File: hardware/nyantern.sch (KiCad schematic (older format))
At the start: 23 parts

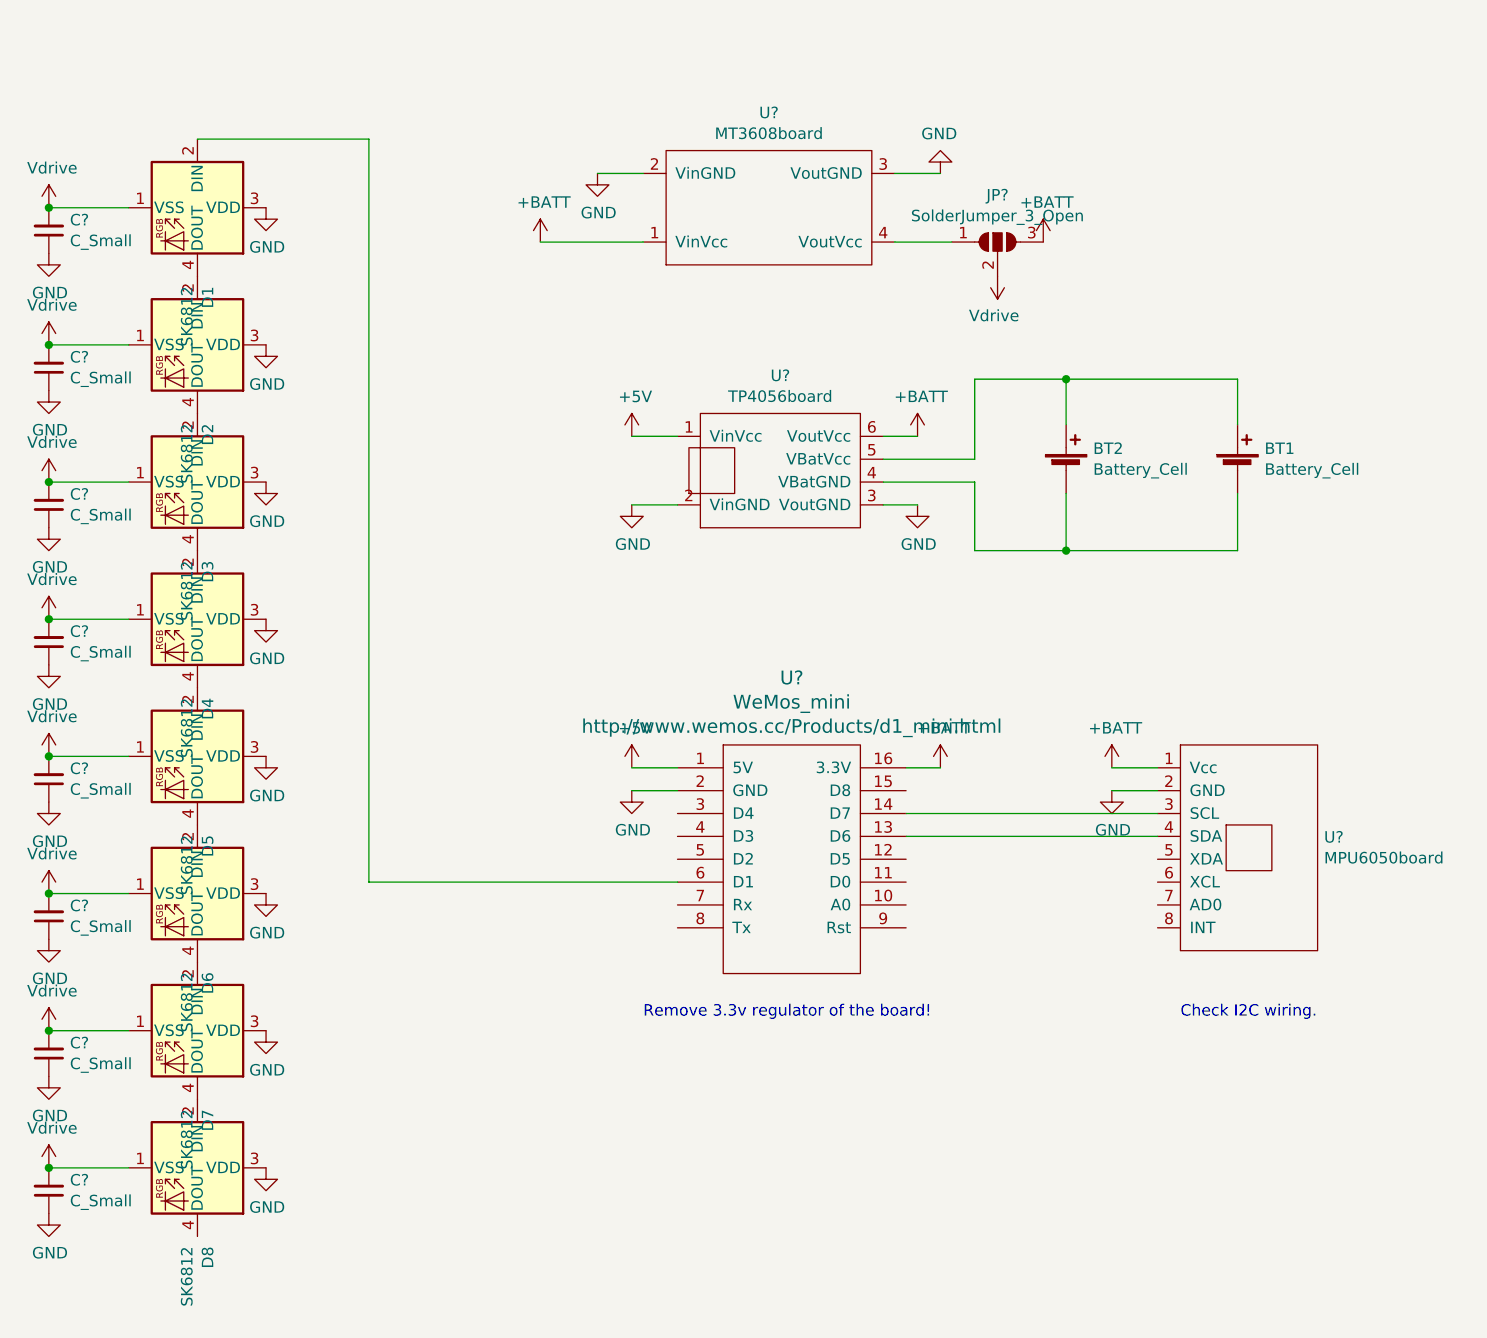
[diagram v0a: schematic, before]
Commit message: Made footprints for modules and put everything on the board
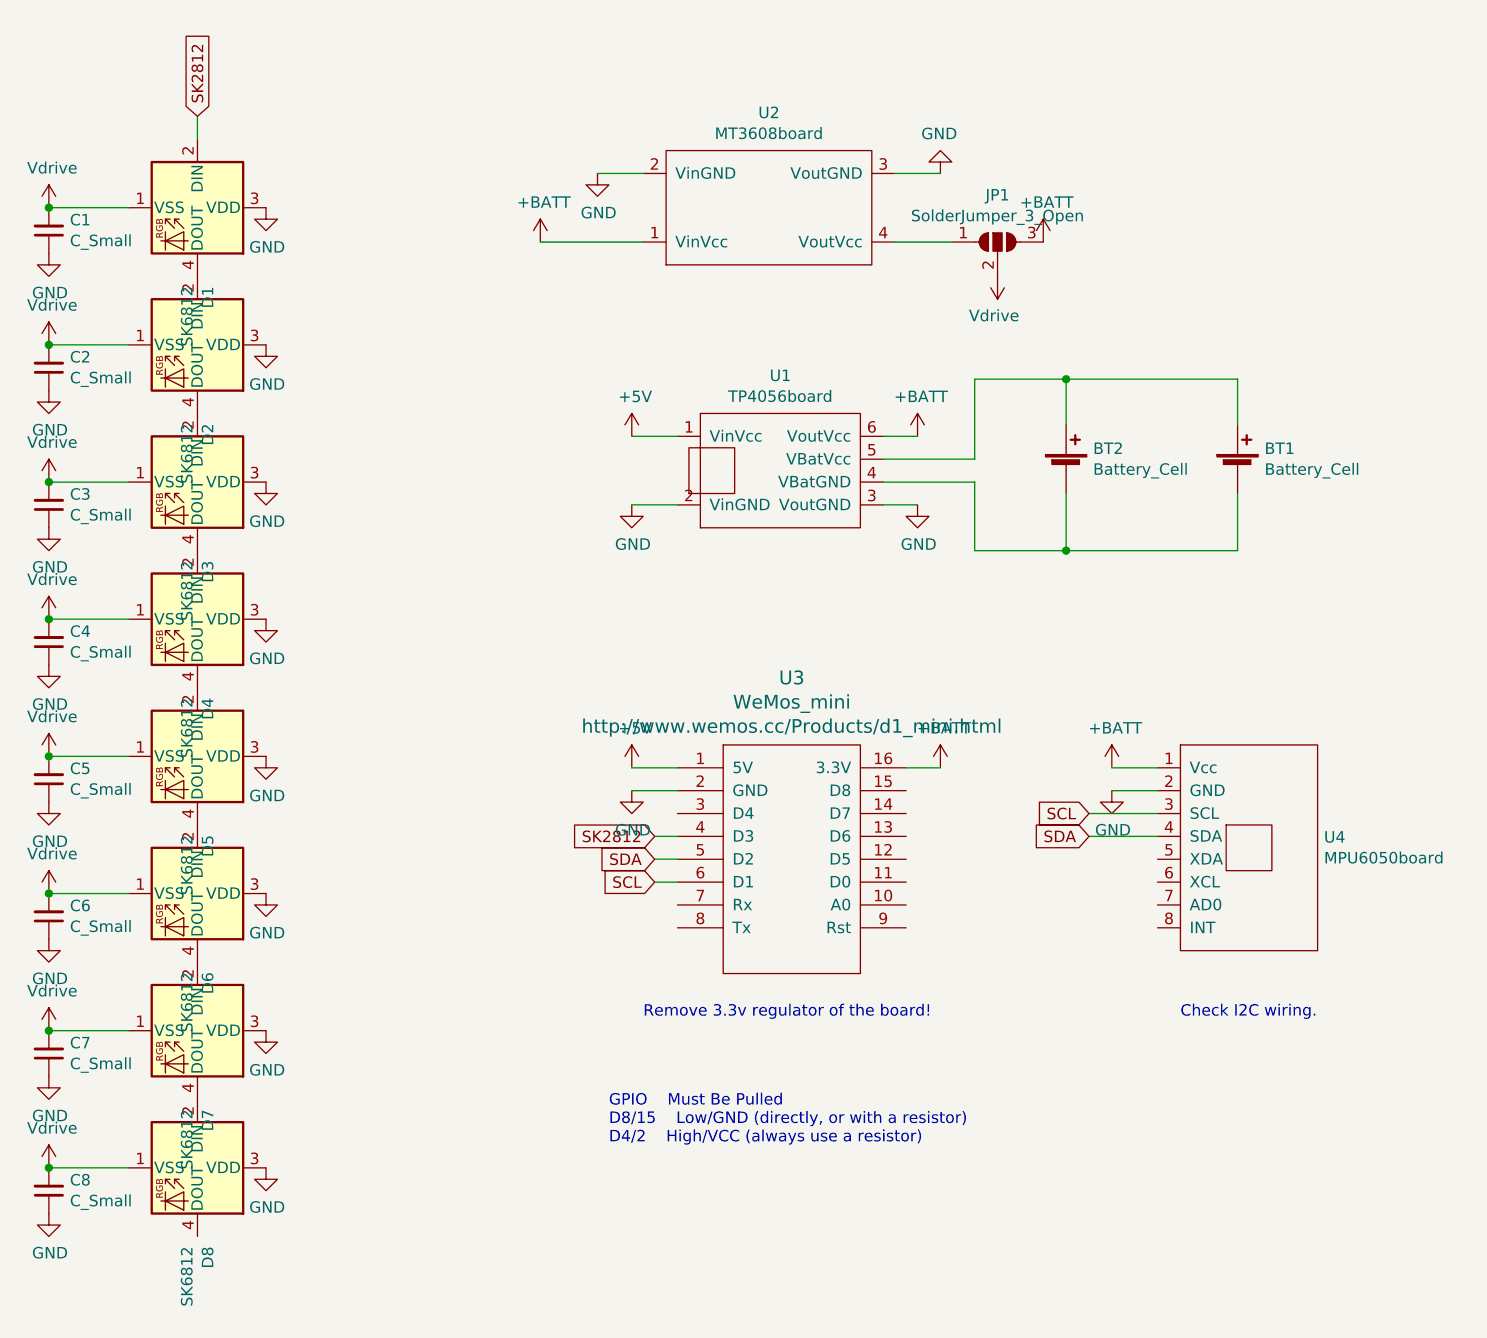
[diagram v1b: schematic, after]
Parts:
- C1, C2, C3, C4, C5, C6, C7, C8: renamed from C?; footprint (none) -> Capacitor_SMD:C_0805_2012Metric
- JP1: renamed from JP?; footprint (none) -> Jumper:SolderJumper-3_P1.3mm_Open_RoundedPad1.0x1.5mm_NumberLabels
- U1: renamed from U?; footprint (none) -> BamboulabFootprints:TP4056board
- U2: renamed from U?; footprint (none) -> BamboulabFootprints:MT3608board
- U3: renamed from U?; footprint (none) -> BamboulabFootprints:D1_mini_board
- U4: renamed from U?; footprint (none) -> Connector_PinHeader_2.54mm:PinHeader_1x08_P2.54mm_Vertical
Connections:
- net SCL: now reaches U3.6 (D1)
- net SCL: now also U4.3 (SCL); no longer D1.2 (DIN)
- net at U3.13 (D6): no longer U4.4 (SDA)
- net at U3.14 (D7): no longer U4.3 (SCL)
- net SK2812: now reaches U3.4 (D3)
- net SK2812: now also D1.2 (DIN)
- net SDA: now reaches U3.5 (D2)
- net SDA: now also U4.4 (SDA)
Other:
- note added: "GPIO Must Be Pulled\nD8/15 Low/GND (directly, or with a resistor)\nD4/2 High/VCC (always use a resistor)"
